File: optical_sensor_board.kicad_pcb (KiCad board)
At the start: 2 copper layers, 67.5 x 45.5 mm, 33 parts, among them J2 Conn_01x09_Socket, U1 PMW3389DM‐T3QU, U3 LM317L_SOT-89

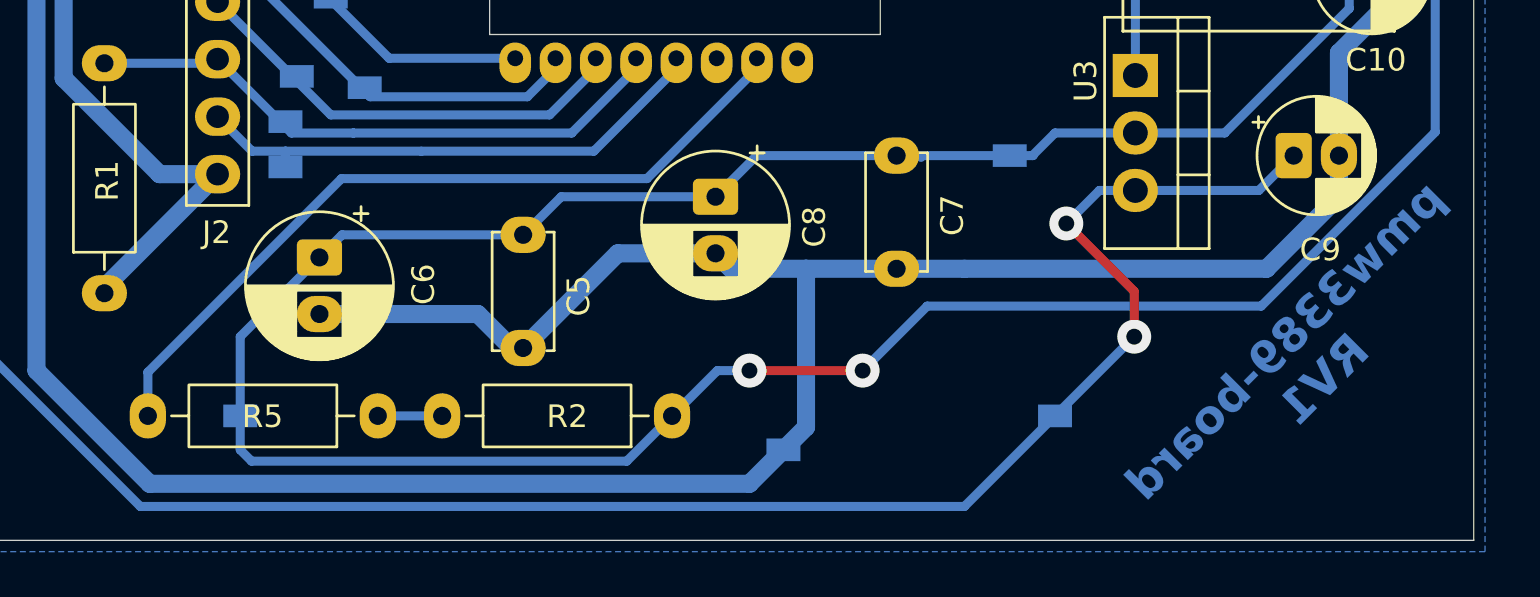
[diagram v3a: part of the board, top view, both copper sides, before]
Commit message: Modificato graficamente lo schematico + moidifiche al PCB
 - Sistemato graficamente lo schema
 - Corretto il testo del PCB
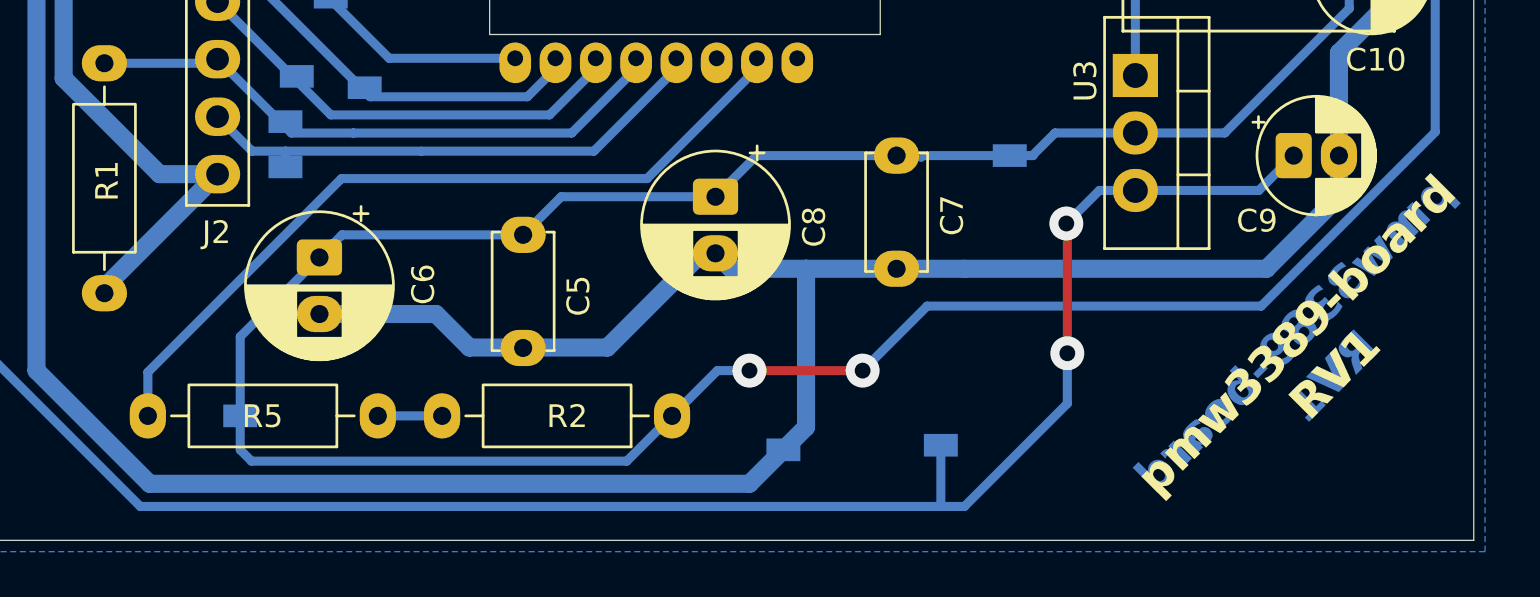
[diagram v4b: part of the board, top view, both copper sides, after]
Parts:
- moved TP4 5.21 mm to (156.0, 98.3)
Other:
- board text added: "RV1"
- board text added: "pmw3389-board"
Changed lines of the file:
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@@
 		(tags "CP Radial series Radial pin pitch 2.00mm diameter 5mm height 7mm Electrolytic Capacitor")
 		(property "Reference" "C9"
-			(at 1.175112 4.162 180)
+			(at -1.618888 2.892 180)
 			(layer "F.SilkS")
 			(effects
@@
 	(footprint "TestPoint:TestPoint_Pad_1.0x1.0mm"
 		(layer "B.Cu")
-		(at 161 97 180)
+		(at 155.956 98.298 180)
 		(descr "SMD rectangular pad as test Point, square 1.0mm side length")
 		(tags "test point SMD pad rectangle square")
 		(property "Reference" "TP4"
-			(at 0 1.448 0)
+			(at 0 1.448001 0)
 			(layer "B.SilkS")
 			(effects
@@
 		)
 		(property "Value" "T_5V"
-			(at 0 -1.55 0)
+			(at 0 -1.550001 0)
 			(layer "B.Fab")
 			(effects
@@
 		(layer "Edge.Cuts")
 	)
-	(gr_text "pmw3389-board\nRV1\n"
-		(at 173.5 96 45)
+	(gr_text "RV1\n"
+		(at 175.514 94.234 45)
+		(layer "B.Cu")
+		(effects
+			(font
+				(size 1.5 1.5)
+				(thickness 0.3)
+				(bold yes)
+			)
+			(justify left bottom mirror)
+		)
+	)
+	(gr_text "pmw3389-board"
+		(at 172.212 93.98 45)
 		(layer "B.Cu")
 		(effects
@@
 		)
 	)
+	(gr_text "pmw3389-board\nRV1\n"
+		(at 173.99 95.758 45)
+		(layer "F.SilkS")
+		(effects
+			(font
+				(size 1.5 1.5)
+				(thickness 0.3)
+				(bold yes)
+			)
+			(justify bottom)
+		)
+	)
 	(segment
 		(start 149.36 63)
@@
 	)
 	(segment
-		(start 150 90.5)
-		(end 146.682379 90.5)
+		(start 118.246 63.754)
+		(end 115.998001 66.001999)
 		(width 0.8)
 		(layer "B.Cu")
@@
 	)
 	(segment
-		(start 173.544888 87.3)
-		(end 173.544888 85.5)
+		(start 150 90.5)
+		(end 146.682379 90.5)
 		(width 0.8)
 		(layer "B.Cu")
@@
 	)
 	(segment
-		(start 135.5 92.5)
-		(end 128.5 92.5)
+		(start 146 89.817621)
+		(end 145.386379 89.817621)
 		(width 0.8)
 		(layer "B.Cu")
@@
 	)
 	(segment
-		(start 118.246 63.754)
-		(end 115.998001 66.001999)
+		(start 173.544888 87.3)
+		(end 173.544888 85.5)
 		(width 0.8)
 		(layer "B.Cu")
@@
 	)
 	(segment
-		(start 121.001 100.001)
-		(end 147.499 100.001)
+		(start 141.224 93.98)
+		(end 137.52 93.98)
 		(width 0.8)
 		(layer "B.Cu")
@@
 	)
 	(segment
-		(start 115.998001 94.998001)
-		(end 121.001 100.001)
+		(start 136.27 68.73)
+		(end 135.27 67.73)
 		(width 0.8)
 		(layer "B.Cu")
@@
 	)
 	(segment
-		(start 136.27 68.73)
-		(end 135.27 67.73)
+		(start 115.998001 94.998001)
+		(end 121.001 100.001)
 		(width 0.8)
 		(layer "B.Cu")
@@
 	)
 	(segment
+		(start 150 97.5)
+		(end 150 90.5)
+		(width 0.8)
+		(layer "B.Cu")
+		(net 2)
+	)
+	(segment
 		(start 156.5 75)
 		(end 156.591189 74.908811)
@@
 	)
 	(segment
-		(start 133.54 66)
-		(end 128.5 66)
+		(start 137.52 93.98)
+		(end 137.5 94)
 		(width 0.8)
 		(layer "B.Cu")
@@
 	)
 	(segment
-		(start 137 94)
-		(end 135.5 92.5)
+		(start 133.54 66)
+		(end 128.5 66)
 		(width 0.8)
 		(layer "B.Cu")
@@
 	)
 	(segment
-		(start 146 89.817621)
-		(end 141.682379 89.817621)
+		(start 146.682379 90.5)
+		(end 146 89.817621)
 		(width 0.8)
 		(layer "B.Cu")
@@
 	)
 	(segment
-		(start 146.682379 90.5)
-		(end 146 89.817621)
+		(start 133.648 92.5)
+		(end 128.5 92.5)
 		(width 0.8)
 		(layer "B.Cu")
@@
 	)
 	(segment
+		(start 119.516 63.754)
+		(end 118.246 63.754)
+		(width 0.8)
+		(layer "B.Cu")
+		(net 2)
+	)
+	(segment
+		(start 147.499 100.001)
+		(end 150 97.5)
+		(width 0.8)
+		(layer "B.Cu")
+		(net 2)
+	)
+	(segment
 		(start 147.978233 65.521767)
 		(end 148 65.5)
@@
 	)
 	(segment
+		(start 145.386379 89.817621)
+		(end 141.224 93.98)
+		(width 0.8)
+		(layer "B.Cu")
+		(net 2)
+	)
+	(segment
 		(start 154 90.5)
 		(end 157 90.5)
@@
 	)
 	(segment
-		(start 119.516 63.754)
-		(end 118.246 63.754)
+		(start 135.128 93.98)
+		(end 133.648 92.5)
 		(width 0.8)
 		(layer "B.Cu")
@@
 	)
 	(segment
-		(start 150 97.5)
-		(end 150 90.5)
+		(start 136.98 93.98)
+		(end 135.128 93.98)
 		(width 0.8)
 		(layer "B.Cu")
@@
 	)
 	(segment
-		(start 147.499 100.001)
-		(end 150 97.5)
+		(start 170 71)
+		(end 171.55 71)
 		(width 0.8)
 		(layer "B.Cu")
@@
 	)
 	(segment
-		(start 170 71)
-		(end 171.55 71)
+		(start 115.998001 66.001999)
+		(end 115.998001 94.998001)
+		(width 0.8)
+		(layer "B.Cu")
+		(net 2)
+	)
+	(segment
+		(start 121.001 100.001)
+		(end 147.499 100.001)
 		(width 0.8)
 		(layer "B.Cu")
@@
 	)
 	(segment
-		(start 137.5 94)
-		(end 137 94)
+		(start 137 94)
+		(end 136.98 93.98)
 		(width 0.8)
 		(layer "B.Cu")
@@
 	)
 	(segment
-		(start 115.998001 66.001999)
-		(end 115.998001 94.998001)
-		(width 0.8)
-		(layer "B.Cu")
-		(net 2)
-	)
-	(segment
 		(start 163.484128 59)
 		(end 159.301 63.183128)
@@
 	)
 	(segment
-		(start 141.682379 89.817621)
-		(end 137.5 94)
+		(start 137.5 94)
+		(end 137 94)
 		(width 0.8)
 		(layer "B.Cu")
@@
 	)
 	(segment
-		(start 114 69.5)
-		(end 120 69.5)
+		(start 161.544 88.544)
+		(end 161.5 88.5)
 		(width 0.4)
 		(layer "F.Cu")
@@
 	)
 	(segment
-		(start 161.5 88.5)
-		(end 164.5 91.5)
+		(start 161.544 94.234)
+		(end 161.544 88.544)
 		(width 0.4)
 		(layer "F.Cu")
@@
 	)
 	(segment
-		(start 164.5 91.5)
-		(end 164.5 93.5)
+		(start 114 69.5)
+		(end 120 69.5)
 		(width 0.4)
 		(layer "F.Cu")
@@
 	)
 	(via
-		(at 164.5 93.5)
+		(at 161.544 94.234)
 		(size 1.5)
 		(drill 0.7)
@@
 	)
 	(segment
-		(start 114 94.415628)
-		(end 114 69.5)
-		(width 0.4)
-		(layer "B.Cu")
-		(net 5)
-	)
-	(segment
 		(start 120.96 68.54)
 		(end 124 68.54)
@@
 	)
 	(segment
-		(start 156.998 101.002)
-		(end 120.586372 101.002)
+		(start 120.586372 101.002)
+		(end 114 94.415628)
 		(width 0.4)
 		(layer "B.Cu")
@@
 	)
 	(segment
-		(start 170.004888 87.04)
-		(end 171.544888 85.5)
+		(start 161.544 94.234)
+		(end 161.544 96.456)
+		(width 0.4)
+		(layer "B.Cu")
+		(net 5)
+	)
+	(segment
+		(start 114 94.415628)
+		(end 114 69.5)
+		(width 0.4)
+		(layer "B.Cu")
+		(net 5)
+	)
+	(segment
+		(start 156.998 101.002)
+		(end 155.956 101.002)
 		(width 0.4)
 		(layer "B.Cu")
@@
 	)
 	(segment
-		(start 164.5 93.5)
+		(start 161.544 96.456)
 		(end 156.998 101.002)
 		(width 0.4)
@@
 	)
 	(segment
+		(start 170.004888 87.04)
+		(end 171.544888 85.5)
+		(width 0.4)
+		(layer "B.Cu")
+		(net 5)
+	)
+	(segment
 		(start 164.55 87.04)
 		(end 162.96 87.04)
@@
 	)
 	(segment
+		(start 155.956 101.002)
+		(end 120.586372 101.002)
+		(width 0.4)
+		(layer "B.Cu")
+		(net 5)
+	)
+	(segment
 		(start 164.55 87.04)
 		(end 170.004888 87.04)
@@
 	)
 	(segment
-		(start 120.586372 101.002)
-		(end 114 94.415628)
+		(start 155.956 98.298)
+		(end 155.956 101.002)
 		(width 0.4)
 		(layer "B.Cu")

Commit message: SilkScreen pin name
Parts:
- added kibuzzard-692FFC30: G***, kibuzzard-692FFC30, F.Cu at (118.2, 73.5)
- added kibuzzard-692FFC6C: G***, kibuzzard-692FFC6C, F.Cu at (119.0, 76.0)
- added kibuzzard-692FFFAD: G***, kibuzzard-692FFFAD, F.Cu at (119.0, 78.5)
- added kibuzzard-692FFFD7: G***, kibuzzard-692FFFD7, F.Cu at (129.5, 71.0)
- added kibuzzard-692FFFF6: G***, kibuzzard-692FFFF6, F.Cu at (129.0, 81.5)
- added kibuzzard-69300011: G***, kibuzzard-69300011, F.Cu at (129.0, 84.0)
- added kibuzzard-69300A7E: G***, kibuzzard-69300A7E, F.Cu at (129.0, 86.5)
- added kibuzzard-69300AAA: G***, kibuzzard-69300AAA, F.Cu at (119.0, 66.0)
- added kibuzzard-69300B41: G***, kibuzzard-69300B41, F.Cu at (119.0, 68.5)
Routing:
- net +5V: track 109.4 -> 108.3 mm

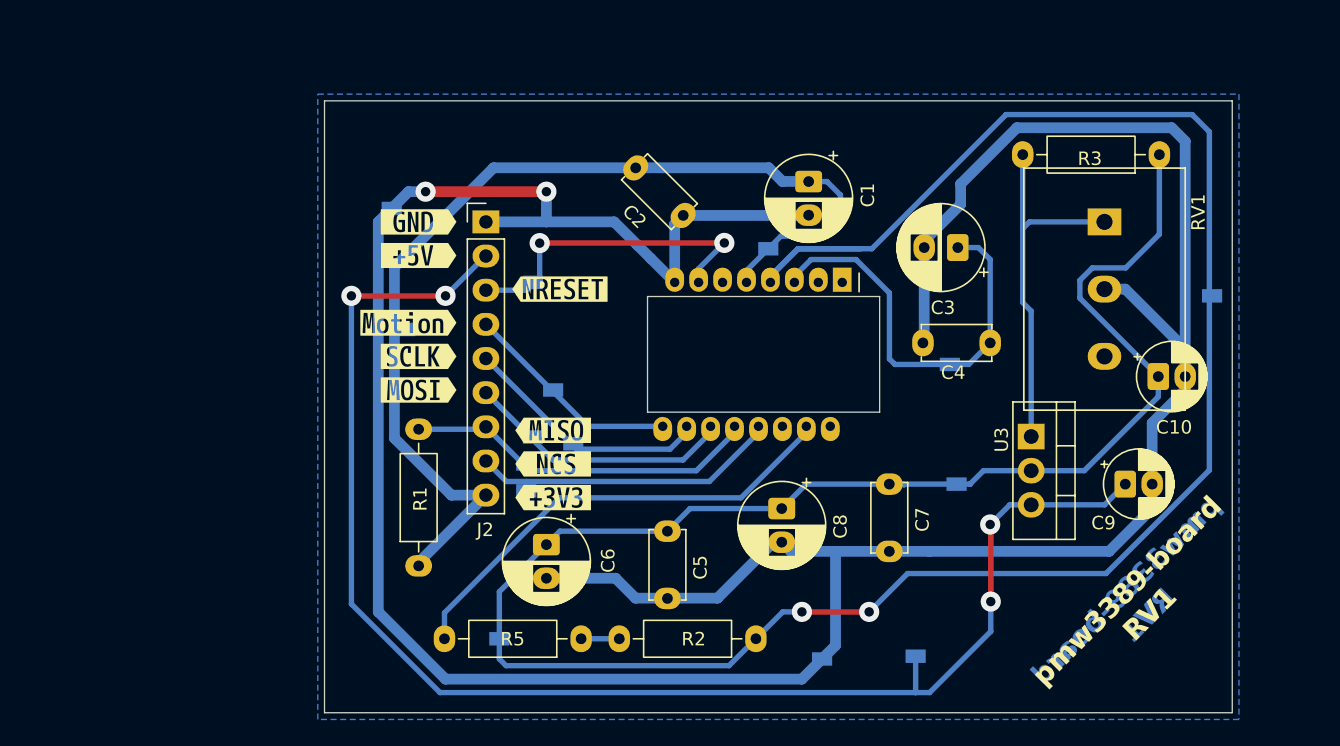
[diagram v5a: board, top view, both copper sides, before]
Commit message: Correct trimmer footprint
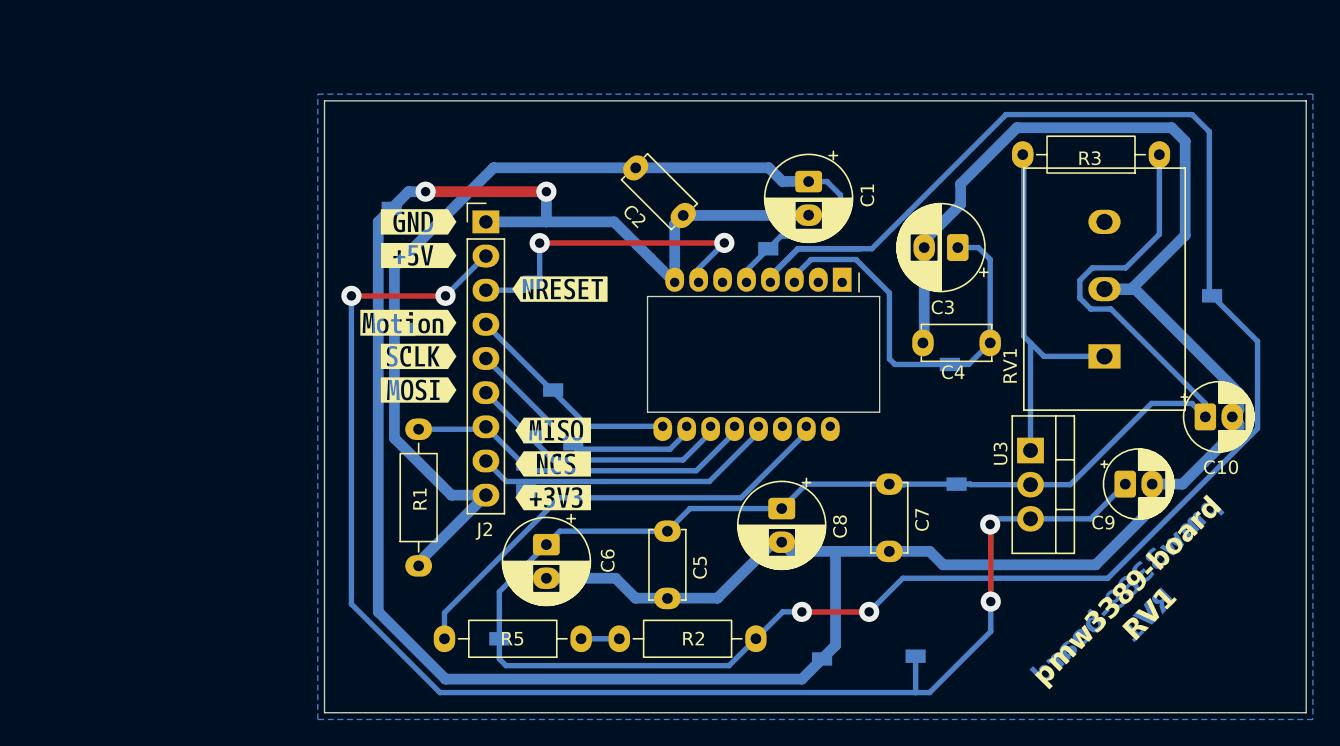
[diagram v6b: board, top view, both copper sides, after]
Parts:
- C9: value 0.1 uF -> 0.1u
- RV1: value 10K_p -> 10K
- moved C10 4.61 mm to (177.5, 80.5)
- moved U3 1.04 mm to (164.5, 83.0)
- turned RV1 to 90 degrees
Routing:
- net VDD: track 217.1 -> 227.2 mm
- net GND: track 238.3 -> 241.8 mm
- net Net-(U3-ADJ): track 27.5 -> 28.9 mm
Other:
- board size 67.5 x 45.5 mm -> 73 x 45.5 mm

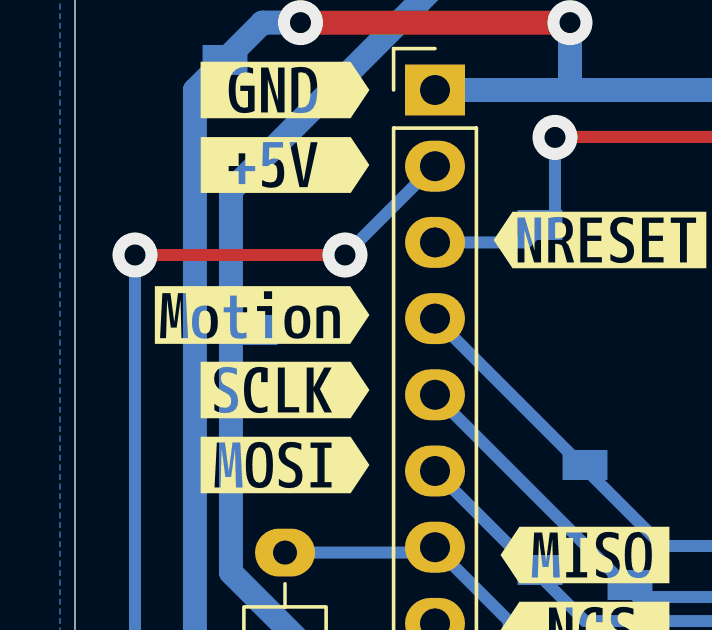
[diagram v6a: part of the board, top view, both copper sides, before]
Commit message: modified SilkScreen for pin MOTION
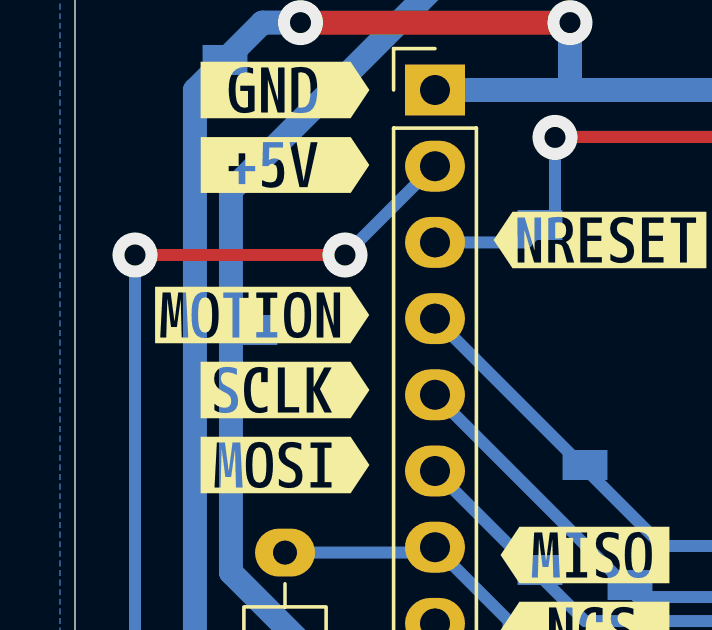
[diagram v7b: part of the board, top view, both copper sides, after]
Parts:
- removed kibuzzard-692FFC30: G***, kibuzzard-692FFC30
- added kibuzzard-69303597: G***, kibuzzard-69303597, F.Cu at (118.2, 73.5)

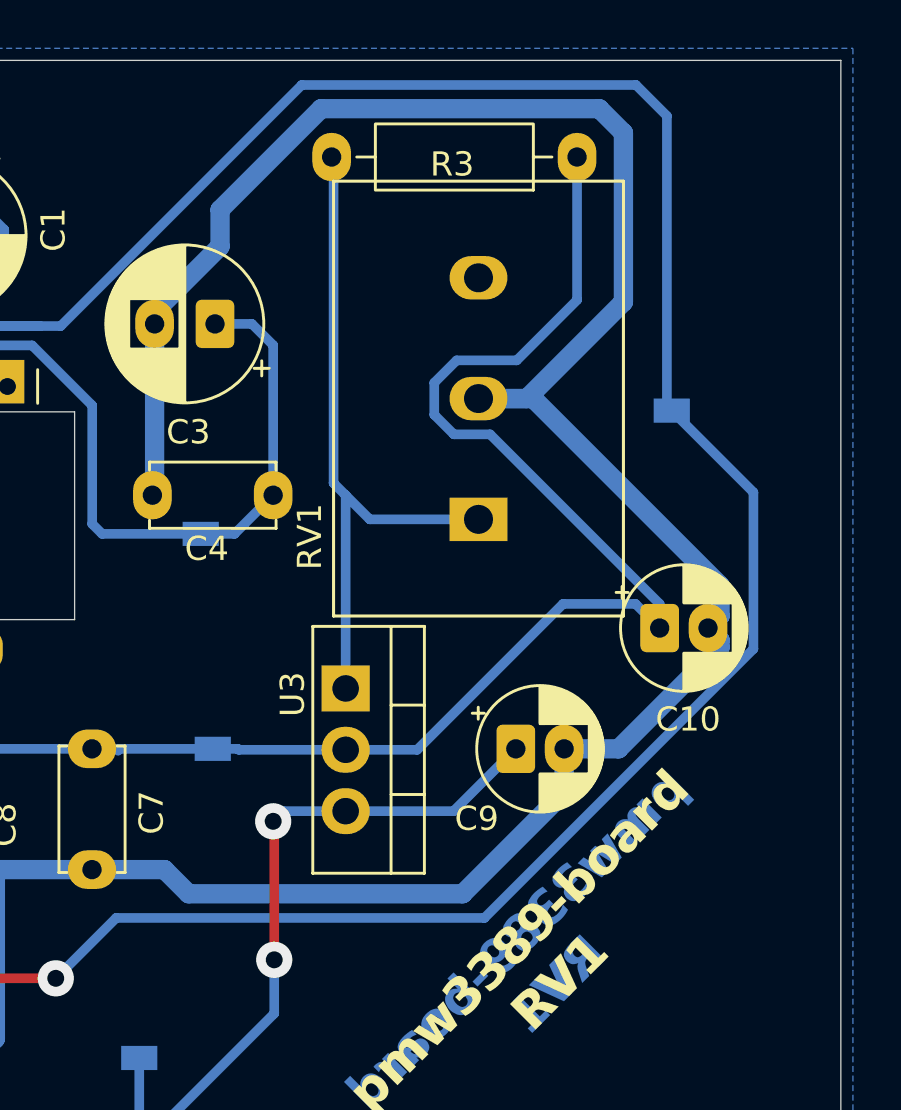
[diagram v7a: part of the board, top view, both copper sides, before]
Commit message: Modified some componets position
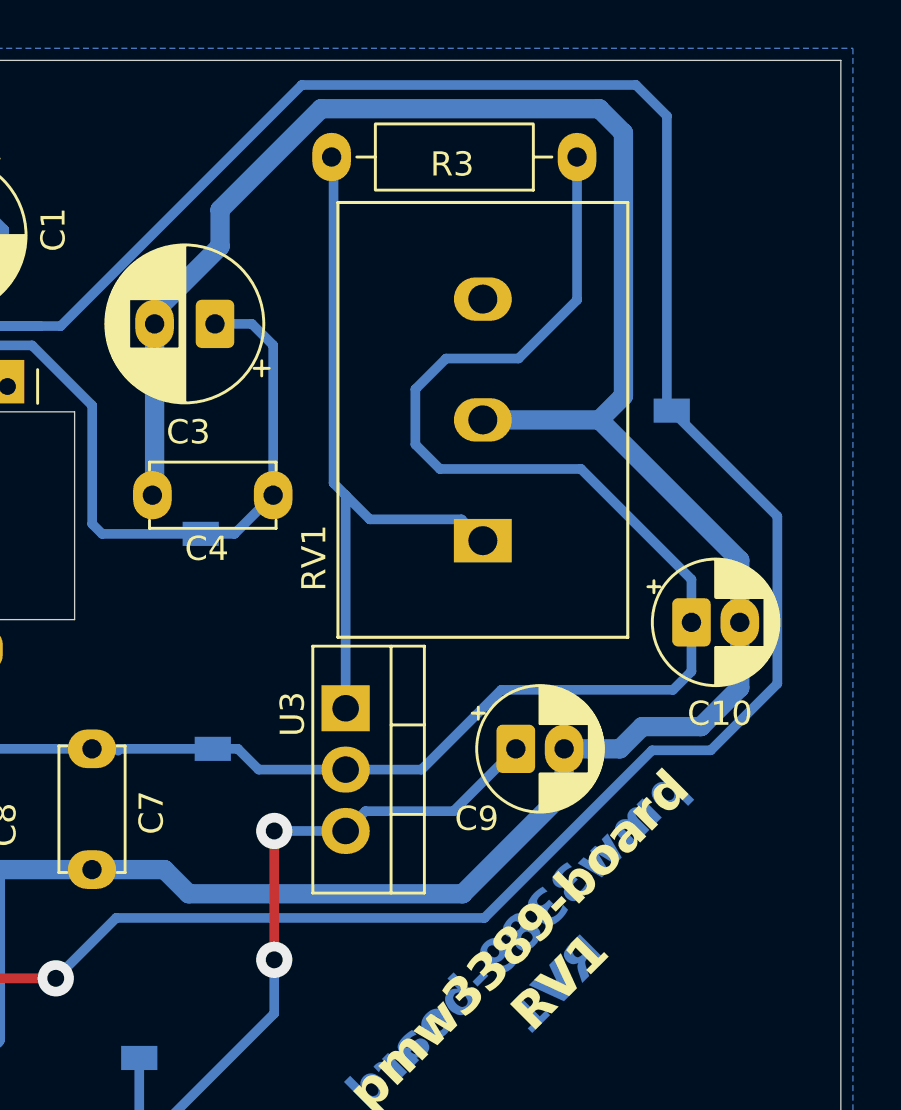
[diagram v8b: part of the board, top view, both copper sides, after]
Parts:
- moved C10 1.34 mm to (178.8, 80.3)
- moved RV1 0.90 mm to (170.2, 71.9)
- moved U3 0.82 mm to (164.5, 83.8)
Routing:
- net VDD: track 227.2 -> 235.7 mm
- net Net-(U3-ADJ): track 28.9 -> 30.2 mm
